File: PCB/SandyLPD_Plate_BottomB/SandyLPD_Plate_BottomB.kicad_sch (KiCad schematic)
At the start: 8 parts

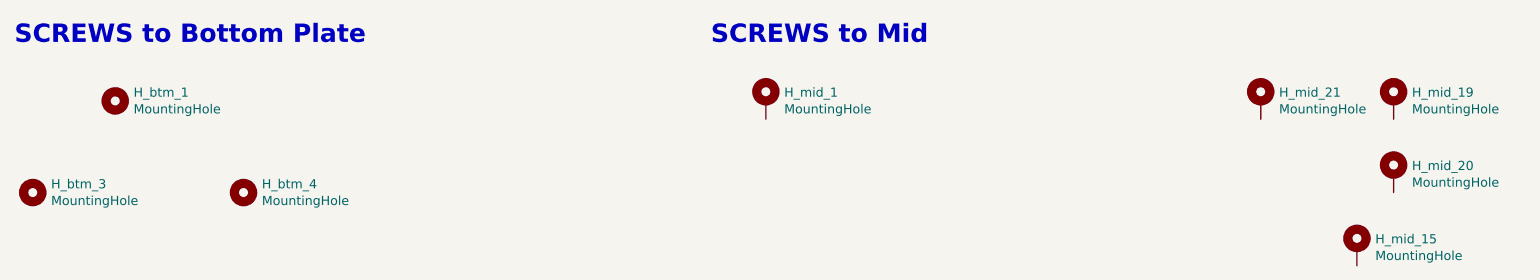
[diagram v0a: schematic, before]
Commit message: ボトムプレートの外形を、基板Baseと同形状に戻す。
仕様では左右端を斜めにして、テント時の小指側持ち上がりを防止する予定だった。
しかし、ケースなどを考慮すると、ボトムの外形が異なると不都合なため、基板Baseと同形状とする。
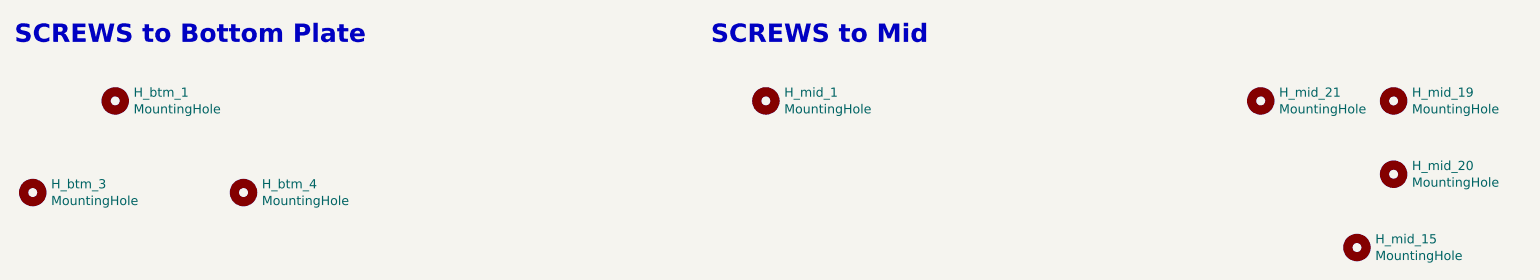
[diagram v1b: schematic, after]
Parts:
- H_mid_1, H_mid_15, H_mid_19, H_mid_20, H_mid_21: symbol Mechanical:MountingHole_Pad -> Mechanical:MountingHole; now left out of the parts list

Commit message: ネジの3Dモデル追加
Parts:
- H_btm_1, H_btm_3, H_btm_4, H_mid_1, H_mid_15, H_mid_19, H_mid_20, H_mid_21: footprint locallib:MountingHole_2.2mm_M2_no_REF -> locallib:MountingHole_2.2mm_M2_no_REF_Plastic_L5mm
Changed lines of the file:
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@@
 			)
 		)
-		(property "Footprint" "locallib:MountingHole_2.2mm_M2_no_REF"
+		(property "Footprint" "locallib:MountingHole_2.2mm_M2_no_REF_Plastic_L5mm"
 			(at 133.35 55.245 0)
 			(effects
@@
 			)
 		)
-		(property "Footprint" "locallib:MountingHole_2.2mm_M2_no_REF"
+		(property "Footprint" "locallib:MountingHole_2.2mm_M2_no_REF_Plastic_L5mm"
 			(at 201.93 55.245 0)
 			(effects
@@
 			)
 		)
-		(property "Footprint" "locallib:MountingHole_2.2mm_M2_no_REF"
+		(property "Footprint" "locallib:MountingHole_2.2mm_M2_no_REF_Plastic_L5mm"
 			(at 60.96 67.945 0)
 			(effects
@@
 			)
 		)
-		(property "Footprint" "locallib:MountingHole_2.2mm_M2_no_REF"
+		(property "Footprint" "locallib:MountingHole_2.2mm_M2_no_REF_Plastic_L5mm"
 			(at 220.345 65.405 0)
 			(effects
@@
 			)
 		)
-		(property "Footprint" "locallib:MountingHole_2.2mm_M2_no_REF"
+		(property "Footprint" "locallib:MountingHole_2.2mm_M2_no_REF_Plastic_L5mm"
 			(at 31.75 67.945 0)
 			(effects
@@
 			)
 		)
-		(property "Footprint" "locallib:MountingHole_2.2mm_M2_no_REF"
+		(property "Footprint" "locallib:MountingHole_2.2mm_M2_no_REF_Plastic_L5mm"
 			(at 215.265 75.565 0)
 			(effects
@@
 			)
 		)
-		(property "Footprint" "locallib:MountingHole_2.2mm_M2_no_REF"
+		(property "Footprint" "locallib:MountingHole_2.2mm_M2_no_REF_Plastic_L5mm"
 			(at 43.18 55.245 0)
 			(effects
@@
 			)
 		)
-		(property "Footprint" "locallib:MountingHole_2.2mm_M2_no_REF"
+		(property "Footprint" "locallib:MountingHole_2.2mm_M2_no_REF_Plastic_L5mm"
 			(at 220.345 55.245 0)
 			(effects
